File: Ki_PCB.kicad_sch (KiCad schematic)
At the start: 9 parts, among them J1 0039301020, J2 B3B-XH-AM(LF)(SN), J3 0039301020, J4 0470531000, J5 4pin JST, SW1 SW_Push

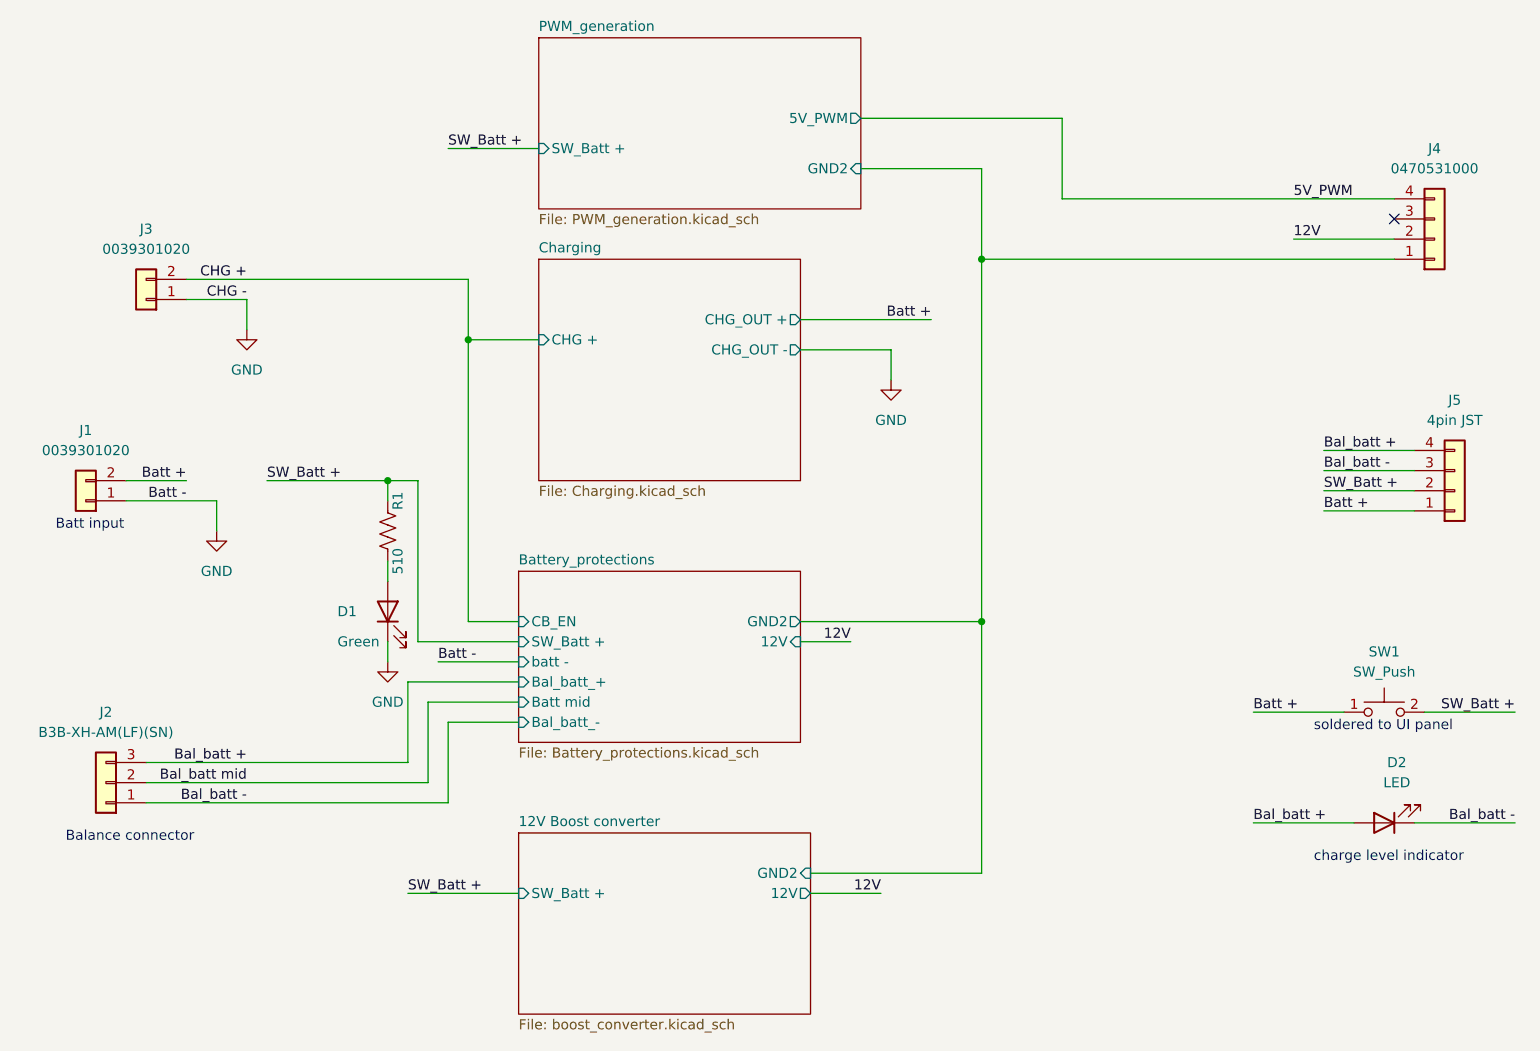
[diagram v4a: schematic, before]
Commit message: layout 1 done, dsr errors with gnd plane clearances
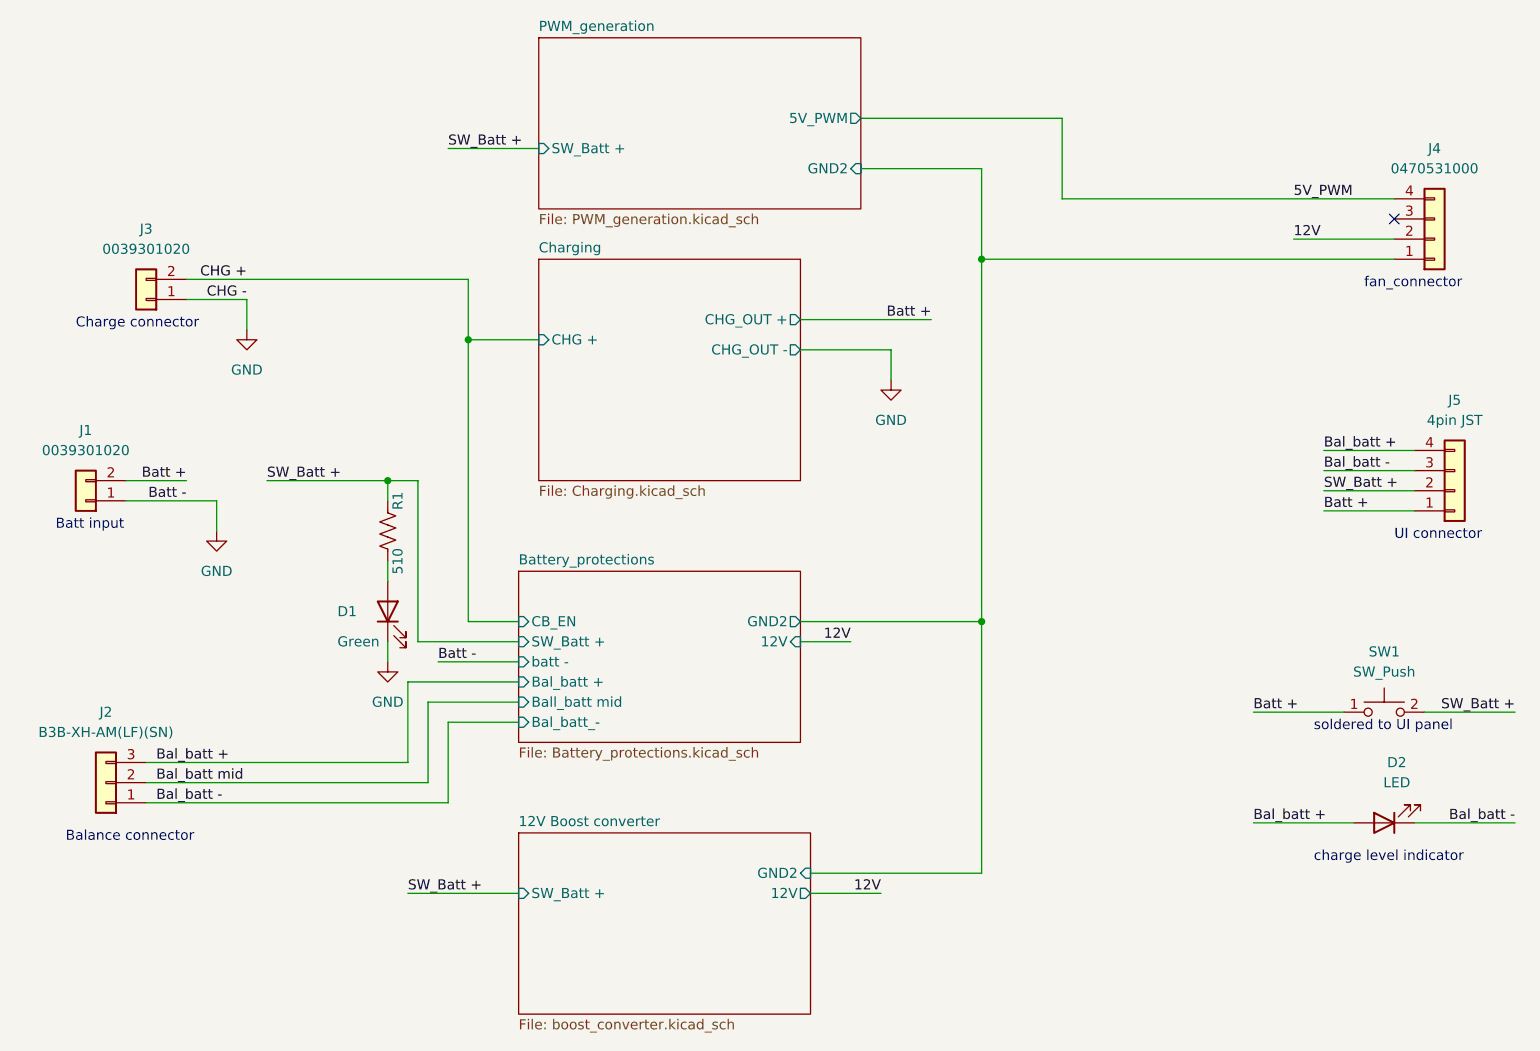
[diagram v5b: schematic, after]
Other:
- sheet Battery_protections ports: added Bal_batt +, Ball_batt mid; removed Bal_batt_+, Batt mid
- note added: "Charge connector"
- note added: "UI connector"
- note added: "fan_connector"
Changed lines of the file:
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@@
+    (stroke (width 0) (type default) (color 0 0 0 0))
+  )
+  (wire (pts (xy 113.03 92.71) (xy 135.89 92.71))
+    (stroke (width 0) (type default) (color 0 0 0 0))
+  )
+  (wire (pts (xy 124.46 62.23) (xy 124.46 58.42))
+    (stroke (width 0) (type default) (color 0 0 0 0))
+  )
+  (wire (pts (xy 170.18 118.11) (xy 182.88 118.11))
+    (stroke (width 0) (type default) (color 0 0 0 0))
+  )
+  (wire (pts (xy 135.89 92.71) (xy 135.89 124.46))
+    (stroke (width 0) (type default) (color 0 0 0 0))
+  )
+  (wire (pts (xy 68.58 115.57) (xy 68.58 105.41))
+    (stroke (width 0) (type default) (color 0 0 0 0))
+  )
+  (wire (pts (xy 71.12 49.53) (xy 71.12 57.15))
+    (stroke (width 0) (type default) (color 0 0 0 0))
+  )
+  (wire (pts (xy 135.89 35.56) (xy 120.65 35.56))
+    (stroke (width 0) (type default) (color 0 0 0 0))
+  )
+  (wire (pts (xy 170.18 104.14) (xy 181.61 104.14))
+    (stroke (width 0) (type default) (color 0 0 0 0))
+  )
+  (wire (pts (xy 30.48 115.57) (xy 68.58 115.57))
+    (stroke (width 0) (type default) (color 0 0 0 0))
+  )
+  (wire (pts (xy 64.77 95.25) (xy 77.47 95.25))
+    (stroke (width 0) (type default) (color 0 0 0 0))
+  )
+  (wire (pts (xy 124.46 58.42) (xy 113.03 58.42))
+    (stroke (width 0) (type default) (color 0 0 0 0))
+  )
+  (wire (pts (xy 113.03 95.25) (xy 119.38 95.25))
+    (stroke (width 0) (type default) (color 0 0 0 0))
+  )
+  (wire (pts (xy 114.3 127) (xy 123.19 127))
+    (stroke (width 0) (type default) (color 0 0 0 0))
+  )
+  (wire (pts (xy 71.12 57.15) (xy 80.01 57.15))
+    (stroke (width 0) (type default) (color 0 0 0 0))
+  )
+  (wire (pts (xy 68.58 33.02) (xy 80.01 33.02))
     (stroke (width 0) (type default) (color 0 0 0 0))
   )
@@
     (stroke (width 0) (type default) (color 0 0 0 0))
   )
-  (wire (pts (xy 113.03 92.71) (xy 135.89 92.71))
-    (stroke (width 0) (type default) (color 0 0 0 0))
-  )
-  (wire (pts (xy 124.46 62.23) (xy 124.46 58.42))
-    (stroke (width 0) (type default) (color 0 0 0 0))
-  )
-  (wire (pts (xy 135.89 92.71) (xy 135.89 124.46))
-    (stroke (width 0) (type default) (color 0 0 0 0))
-  )
-  (wire (pts (xy 68.58 115.57) (xy 68.58 105.41))
-    (stroke (width 0) (type default) (color 0 0 0 0))
-  )
-  (wire (pts (xy 170.18 118.11) (xy 182.88 118.11))
-    (stroke (width 0) (type default) (color 0 0 0 0))
-  )
-  (wire (pts (xy 71.12 49.53) (xy 71.12 57.15))
-    (stroke (width 0) (type default) (color 0 0 0 0))
-  )
-  (wire (pts (xy 135.89 35.56) (xy 120.65 35.56))
-    (stroke (width 0) (type default) (color 0 0 0 0))
-  )
-  (wire (pts (xy 170.18 104.14) (xy 181.61 104.14))
-    (stroke (width 0) (type default) (color 0 0 0 0))
-  )
-  (wire (pts (xy 30.48 115.57) (xy 68.58 115.57))
-    (stroke (width 0) (type default) (color 0 0 0 0))
-  )
-  (wire (pts (xy 64.77 95.25) (xy 77.47 95.25))
-    (stroke (width 0) (type default) (color 0 0 0 0))
-  )
-  (wire (pts (xy 124.46 58.42) (xy 113.03 58.42))
-    (stroke (width 0) (type default) (color 0 0 0 0))
-  )
-  (wire (pts (xy 113.03 95.25) (xy 119.38 95.25))
-    (stroke (width 0) (type default) (color 0 0 0 0))
-  )
-  (wire (pts (xy 114.3 127) (xy 123.19 127))
-    (stroke (width 0) (type default) (color 0 0 0 0))
-  )
-  (wire (pts (xy 71.12 57.15) (xy 80.01 57.15))
-    (stroke (width 0) (type default) (color 0 0 0 0))
-  )
-  (wire (pts (xy 68.58 33.02) (xy 80.01 33.02))
-    (stroke (width 0) (type default) (color 0 0 0 0))
-  )
   (wire (pts (xy 67.31 97.79) (xy 77.47 97.79))
     (stroke (width 0) (type default) (color 0 0 0 0))
@@
     (stroke (width 0) (type default) (color 0 0 0 0))
   )
+  (wire (pts (xy 63.5 127) (xy 77.47 127))
+    (stroke (width 0) (type default) (color 0 0 0 0))
+  )
+  (wire (pts (xy 64.77 74.93) (xy 64.77 95.25))
+    (stroke (width 0) (type default) (color 0 0 0 0))
+  )
+  (wire (pts (xy 63.5 100.33) (xy 63.5 110.49))
+    (stroke (width 0) (type default) (color 0 0 0 0))
+  )
+  (wire (pts (xy 43.18 52.07) (xy 43.18 55.88))
+    (stroke (width 0) (type default) (color 0 0 0 0))
+  )
   (wire (pts (xy 179.07 71.12) (xy 190.5 71.12))
     (stroke (width 0) (type default) (color 0 0 0 0))
   )
-  (wire (pts (xy 63.5 127) (xy 77.47 127))
-    (stroke (width 0) (type default) (color 0 0 0 0))
-  )
-  (wire (pts (xy 64.77 74.93) (xy 64.77 95.25))
-    (stroke (width 0) (type default) (color 0 0 0 0))
-  )
-  (wire (pts (xy 63.5 100.33) (xy 63.5 110.49))
-    (stroke (width 0) (type default) (color 0 0 0 0))
-  )
-  (wire (pts (xy 43.18 52.07) (xy 43.18 55.88))
-    (stroke (width 0) (type default) (color 0 0 0 0))
-  )
   (wire (pts (xy 146.05 29.21) (xy 146.05 39.37))
     (stroke (width 0) (type default) (color 0 0 0 0))
@@
     (stroke (width 0) (type default) (color 0 0 0 0))
   )
+  (text "fan_connector\n" (at 184.15 50.8 0)
+    (effects (font (size 1.27 1.27)) (justify left bottom))
+  )
   (text "Batt input" (at 19.05 81.28 0)
     (effects (font (size 1.27 1.27)) (justify left bottom))
@@
     (effects (font (size 1.27 1.27)) (justify left bottom))
   )
+  (text "Charge connector\n" (at 21.59 55.88 0)
+    (effects (font (size 1.27 1.27)) (justify left bottom))
+  )
+  (text "UI connector\n" (at 187.96 82.55 0)
+    (effects (font (size 1.27 1.27)) (justify left bottom))
+  )
   (text "charge level indicator\n" (at 177.8 123.19 0)
     (effects (font (size 1.27 1.27)) (justify left bottom))
@@
     (effects (font (size 1.27 1.27)) (justify right bottom))
   )
-  (label "Bal_batt mid" (at 43.18 113.03 180)
-    (effects (font (size 1.27 1.27)) (justify right bottom))
+  (label "Bal_batt mid" (at 31.75 113.03 0)
+    (effects (font (size 1.27 1.27)) (justify left bottom))
   )
   (label "CHG -" (at 43.18 52.07 180)
@@
     (effects (font (size 1.27 1.27)) (justify left bottom))
   )
+  (label "Batt +" (at 170.18 104.14 0)
+    (effects (font (size 1.27 1.27)) (justify left bottom))
+  )
+  (label "Bal_batt +" (at 31.75 110.49 0)
+    (effects (font (size 1.27 1.27)) (justify left bottom))
+  )
+  (label "CHG +" (at 43.18 49.53 180)
+    (effects (font (size 1.27 1.27)) (justify right bottom))
+  )
+  (label "SW_Batt +" (at 45.72 74.93 0)
+    (effects (font (size 1.27 1.27)) (justify left bottom))
+  )
+  (label "Batt +" (at 35.56 74.93 180)
+    (effects (font (size 1.27 1.27)) (justify right bottom))
+  )
+  (label "Bal_batt -" (at 31.75 115.57 0)
+    (effects (font (size 1.27 1.27)) (justify left bottom))
+  )
+  (label "SW_Batt +" (at 179.07 76.2 0)
+    (effects (font (size 1.27 1.27)) (justify left bottom))
+  )
+  (label "Batt +" (at 179.07 78.74 0)
+    (effects (font (size 1.27 1.27)) (justify left bottom))
+  )
   (label "Bal_batt +" (at 179.07 71.12 0)
     (effects (font (size 1.27 1.27)) (justify left bottom))
   )
-  (label "Batt +" (at 170.18 104.14 0)
-    (effects (font (size 1.27 1.27)) (justify left bottom))
-  )
-  (label "CHG +" (at 43.18 49.53 180)
-    (effects (font (size 1.27 1.27)) (justify right bottom))
-  )
-  (label "SW_Batt +" (at 45.72 74.93 0)
-    (effects (font (size 1.27 1.27)) (justify left bottom))
-  )
-  (label "Batt +" (at 35.56 74.93 180)
-    (effects (font (size 1.27 1.27)) (justify right bottom))
-  )
-  (label "Bal_batt +" (at 43.18 110.49 180)
-    (effects (font (size 1.27 1.27)) (justify right bottom))
-  )
-  (label "Bal_batt -" (at 43.18 115.57 180)
-    (effects (font (size 1.27 1.27)) (justify right bottom))
-  )
-  (label "SW_Batt +" (at 179.07 76.2 0)
-    (effects (font (size 1.27 1.27)) (justify left bottom))
-  )
-  (label "Batt +" (at 179.07 78.74 0)
-    (effects (font (size 1.27 1.27)) (justify left bottom))
-  )
   (label "5V_PWM" (at 175.26 39.37 0)
     (effects (font (size 1.27 1.27)) (justify left bottom))
@@
     (effects (font (size 1.27 1.27)) (justify right bottom))
   )
+  (label "SW_Batt +" (at 63.5 127 0)
+    (effects (font (size 1.27 1.27)) (justify left bottom))
+  )
+  (label "12V" (at 119.38 95.25 180)
+    (effects (font (size 1.27 1.27)) (justify right bottom))
+  )
   (label "Bal_batt +" (at 170.18 118.11 0)
     (effects (font (size 1.27 1.27)) (justify left bottom))
-  )
-  (label "SW_Batt +" (at 63.5 127 0)
-    (effects (font (size 1.27 1.27)) (justify left bottom))
-  )
-  (label "12V" (at 119.38 95.25 180)
-    (effects (font (size 1.27 1.27)) (justify right bottom))
   )
   (symbol (lib_id "Device:LED") (at 60.96 91.44 90) (unit 1)
@@
       (effects (font (size 1.27 1.27)) (justify left))
     )
-    (pin "Batt mid" input (at 77.47 102.87 180)
+    (pin "Ball_batt mid" input (at 77.47 102.87 180)
       (effects (font (size 1.27 1.27)) (justify left))
     )
@@
       (effects (font (size 1.27 1.27)) (justify right))
     )
-    (pin "Bal_batt_+" input (at 77.47 100.33 180)
-      (effects (font (size 1.27 1.27)) (justify left))
-    )
+    (pin "Bal_batt +" input (at 77.47 100.33 180)
+      (effects (font (size 1.27 1.27)) (justify left))
+    )

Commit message: 1st Gerber creatd  Please enter the commit message for your changes. Lines starting
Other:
- sheet Battery_protections ports: added Bal_batt mid; removed Ball_batt mid
